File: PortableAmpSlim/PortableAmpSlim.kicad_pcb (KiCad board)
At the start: 2 copper layers, 5 x 30 mm, 20 parts, among them J1 Conn_01x04_Male, J2 Speaker, Q1 MPF102, SW1 Power, U1 LM386

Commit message: Finalized slim portable amp and plotted Gerber files
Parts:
- moved SW1 80.3 mm to (155.2, 83.3), turned to 90 degrees
- moved D1 62.3 mm to (129.0, 81.0)
- moved R1 55.4 mm to (139.2, 77.7), turned to 180 degrees
- moved R2 55.2 mm to (139.2, 74.4), turned to 180 degrees
- moved R3 53.1 mm to (139.2, 71.1), turned to 180 degrees
- moved C3 52.8 mm to (122.7, 76.7), turned to 180 degrees
- moved C2 50.1 mm to (122.7, 67.3), turned to 180 degrees
- moved Q1 43.4 mm to (147.1, 80.8), turned to 180 degrees
- moved C5 37.0 mm to (138.9, 67.3), turned to 180 degrees
- moved H1 33.8 mm to (103.0, 62.0)
- moved H2 31.4 mm to (103.0, 82.0)
- moved C4 30.9 mm to (130.8, 67.3), turned to 180 degrees
- moved C1 27.3 mm to (109.2, 64.8)
- moved U1 15.8 mm to (142.5, 69.1)
- moved RV2 12.3 mm to (154.7, 70.1)
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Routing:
- net Net-(C1-Pad1): track 0.00 -> 56.4 mm
- net Net-(C2-Pad2): track 0.00 -> 35.9 mm
- net Net-(C3-Pad2): track 0.00 -> 34.7 mm
- net Input: track 0.00 -> 30.6 mm
- net Net-(C2-Pad1): track 0.00 -> 30.1 mm
- net Net-(C5-Pad2): track 0.00 -> 23.6 mm
- net Net-(RV2-Pad2): track 0.00 -> 23.4 mm
- net Net-(D1-Pad2): track 0.00 -> 20.6 mm
- net Net-(C5-Pad1): track 0.00 -> 16.8 mm
- net Net-(RV1-Pad2): track 0.00 -> 13.0 mm
- net 9V: track 0.00 -> 12.9 mm
- net Net-(RV2-Pad1): track 0.00 -> 4.99 mm
- net Net-(C4-Pad1): track 0.00 -> 4.15 mm
- added copper zone on B.Cu, net GND
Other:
- board size 5 x 30 mm -> 72 x 30 mm
- board text added: "+"
- board text added: "-"
- board text added: "9V"
- board text added: "GND"
- board text added: "IN"
- board text added: "JLCJLCJLCJLC"
- board text added: "Output"
- board text added: "Thomas McDonagh Slim Portable Amp V1.0 mcdonaghcorp.com"

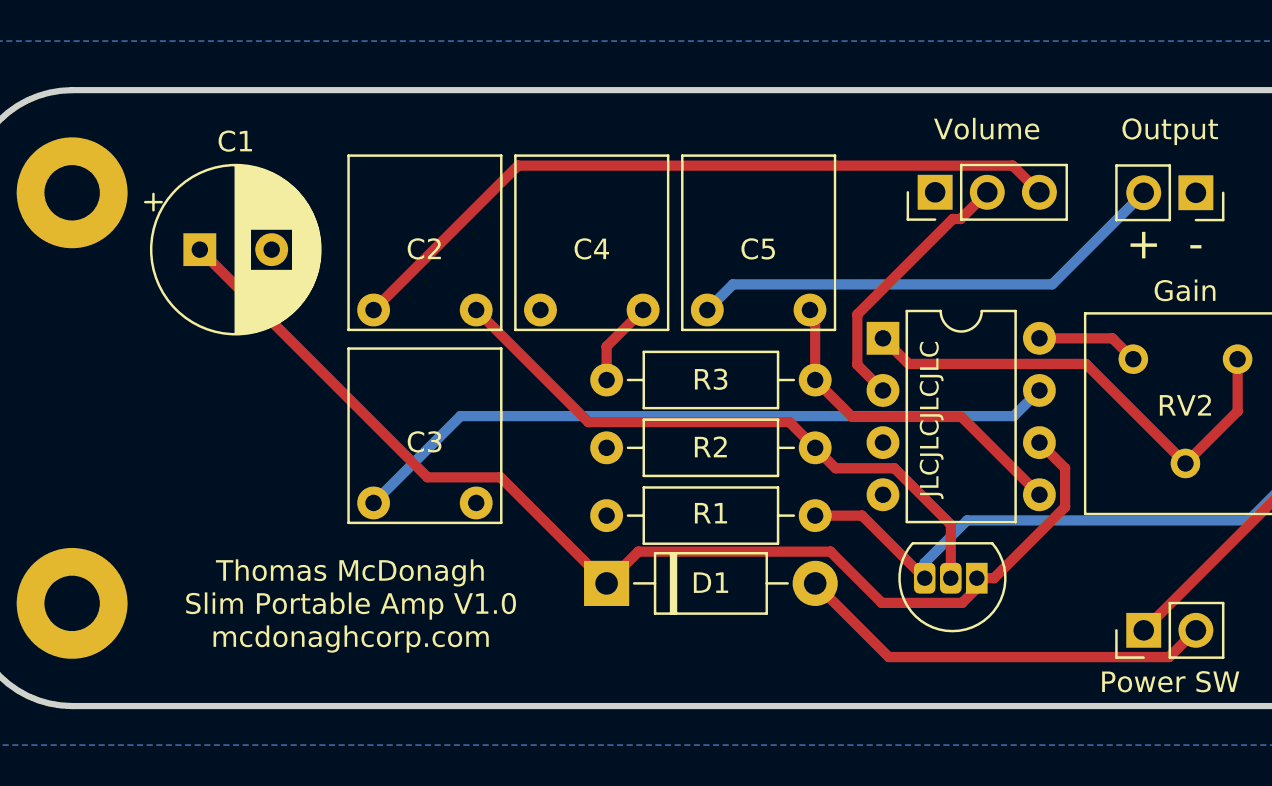
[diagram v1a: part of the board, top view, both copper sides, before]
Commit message: Fixed footprints and replotted Gerber files
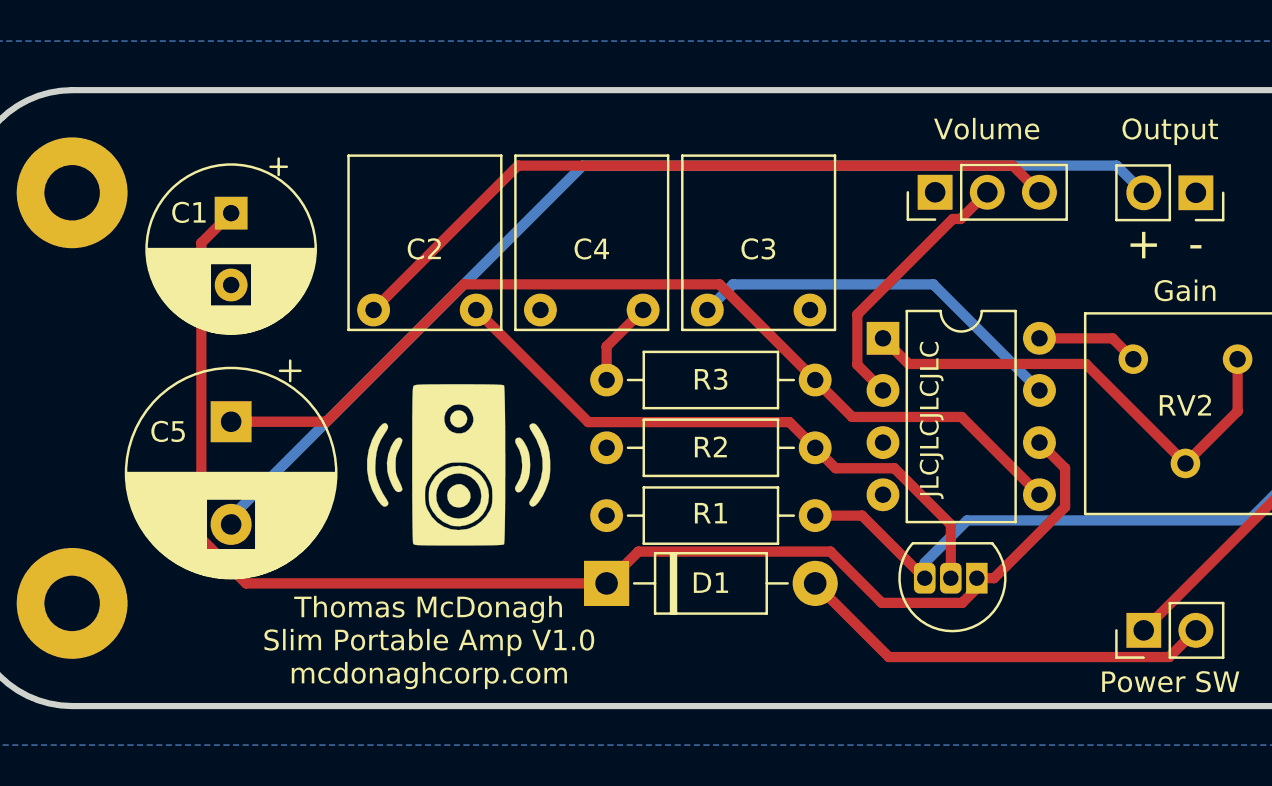
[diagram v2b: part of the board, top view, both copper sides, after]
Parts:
- added G***: LOGO, libraries:speakerIcon, F.Cu at (121.9, 74.9)
- C5: footprint libraries:C_Flat_L7.2_H6.5 -> Capacitor_THT:CP_Radial_D10.0mm_P5.00mm
- moved C5 28.8 mm to (110.7, 73.2), turned to 270 degrees
- moved C3 18.8 mm to (138.9, 67.3)
- moved C1 2.34 mm to (110.7, 63.0), turned to 270 degrees
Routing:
- net Net-(C5-Pad1): track 16.8 -> 46.4 mm
- net Net-(C5-Pad2): track 23.6 -> 52.4 mm
- net Net-(C3-Pad2): track 34.7 -> 18.8 mm
- net Net-(C1-Pad1): track 56.4 -> 67.0 mm

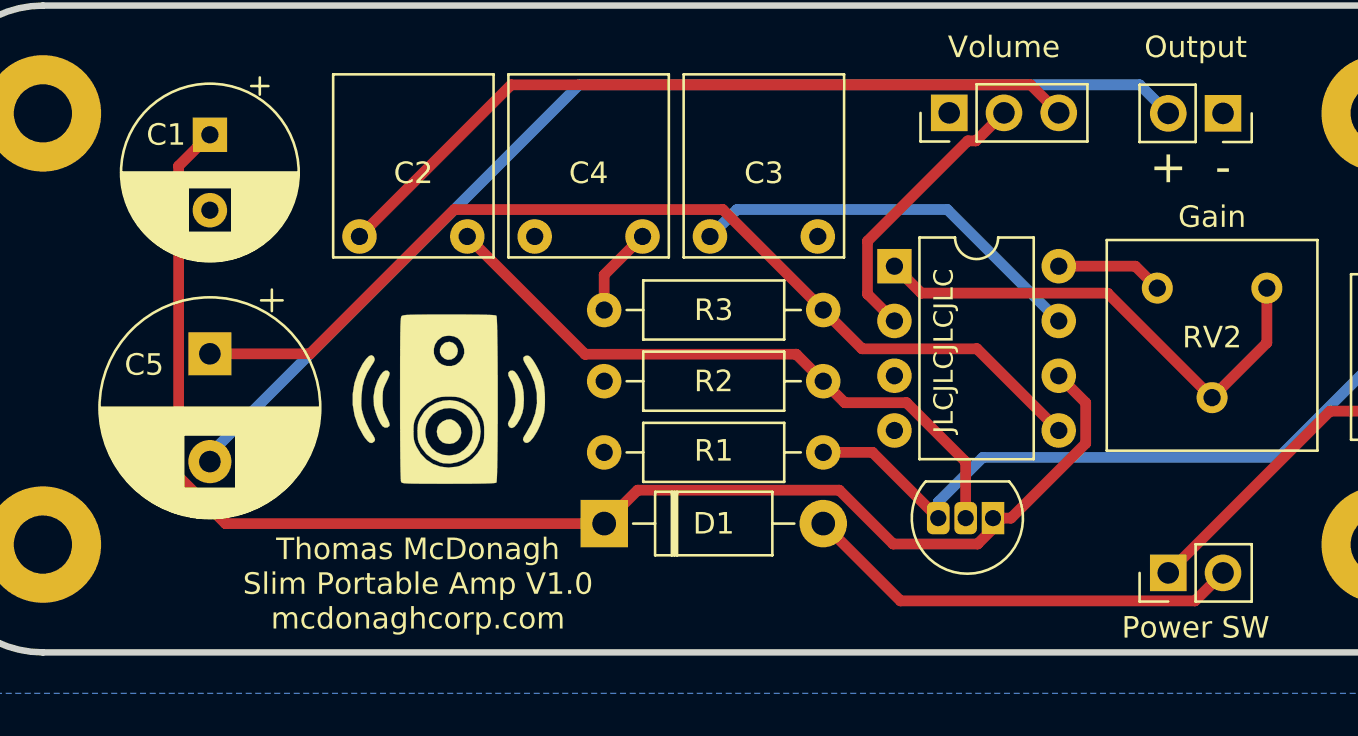
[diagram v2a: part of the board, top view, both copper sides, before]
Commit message: Added LED
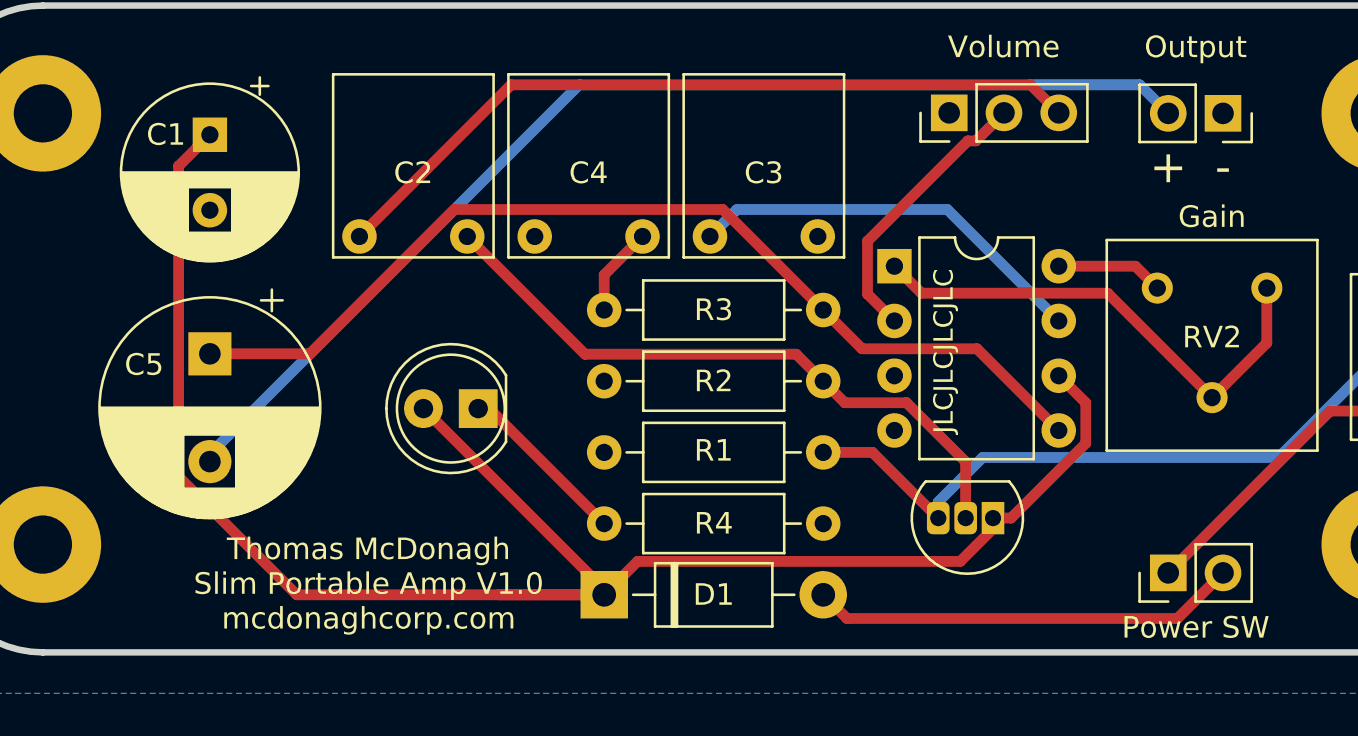
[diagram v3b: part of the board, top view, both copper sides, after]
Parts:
- removed G***: LOGO, libraries:speakerIcon
- added D2: LED, LED_THT:LED_D5.0mm, F.Cu at (123.2, 75.7)
- added R4: 100K, Resistor_THT:R_Axial_DIN0207_L6.3mm_D2.5mm_P10.16mm_Horizontal, F.Cu at (139.2, 81.0)
- moved D1 3.30 mm to (129.0, 84.3)
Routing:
- net Net-(C1-Pad1): track 67.0 -> 84.7 mm
- net Net-(D2-Pad1): track 0.00 -> 8.05 mm
- net Net-(D1-Pad2): track 20.6 -> 19.9 mm
